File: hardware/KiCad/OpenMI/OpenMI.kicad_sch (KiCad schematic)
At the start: 0 parts

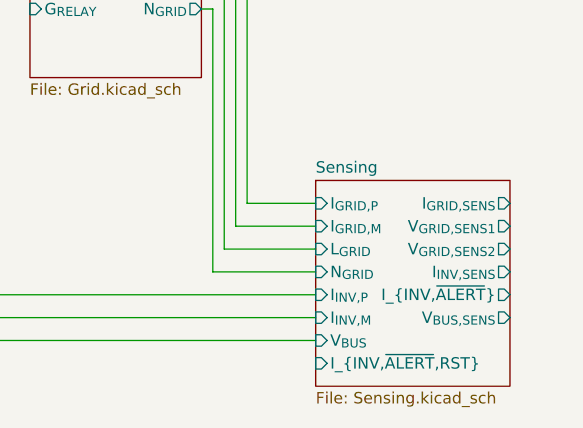
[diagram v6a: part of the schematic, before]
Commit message: feat(hw): Adds grid current alert output to `Sensing`.
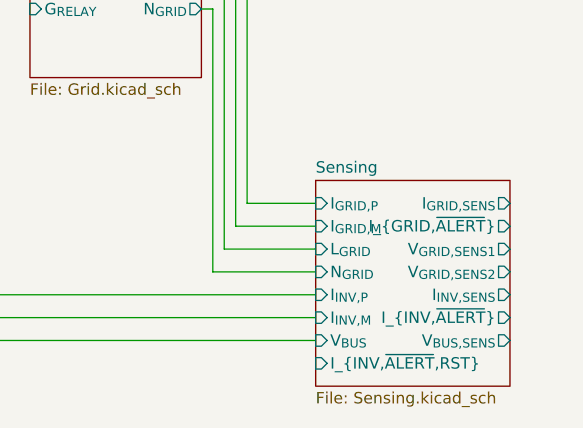
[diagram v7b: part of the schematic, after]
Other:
- sheet Sensing ports: added I_{GRID,~{ALERT}}; removed none
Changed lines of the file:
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@@
       (effects (font (size 1.27 1.27)) (justify left))
     )
-    (pin "I_{INV,~{ALERT}}" output (at 200.66 120.65 0)
+    (pin "I_{INV,~{ALERT}}" output (at 200.66 123.19 0)
       (effects (font (size 1.27 1.27)) (justify right))
     )
@@
       (effects (font (size 1.27 1.27)) (justify left))
     )
-    (pin "I_{INV,SENS}" output (at 200.66 118.11 0)
+    (pin "I_{INV,SENS}" output (at 200.66 120.65 0)
       (effects (font (size 1.27 1.27)) (justify right))
     )
@@
       (effects (font (size 1.27 1.27)) (justify left))
     )
-    (pin "V_{BUS,SENS}" output (at 200.66 123.19 0)
+    (pin "V_{BUS,SENS}" output (at 200.66 125.73 0)
       (effects (font (size 1.27 1.27)) (justify right))
     )
@@
       (effects (font (size 1.27 1.27)) (justify left))
     )
-    (pin "V_{GRID,SENS1}" output (at 200.66 113.03 0)
+    (pin "V_{GRID,SENS1}" output (at 200.66 115.57 0)
       (effects (font (size 1.27 1.27)) (justify right))
     )
-    (pin "V_{GRID,SENS2}" output (at 200.66 115.57 0)
+    (pin "V_{GRID,SENS2}" output (at 200.66 118.11 0)
       (effects (font (size 1.27 1.27)) (justify right))
     )
@@
       (effects (font (size 1.27 1.27)) (justify left))
     )
+    (pin "I_{GRID,~{ALERT}}" output (at 200.66 113.03 0)
+      (effects (font (size 1.27 1.27)) (justify right))
+    )
     (instances

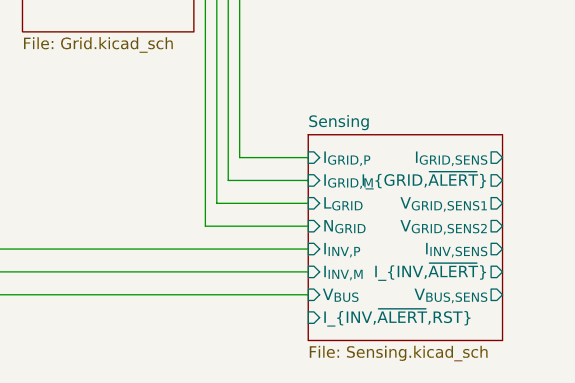
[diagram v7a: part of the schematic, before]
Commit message: feat(hw): Adds zero-crossing-detection (ZCD) to `Sensing`.
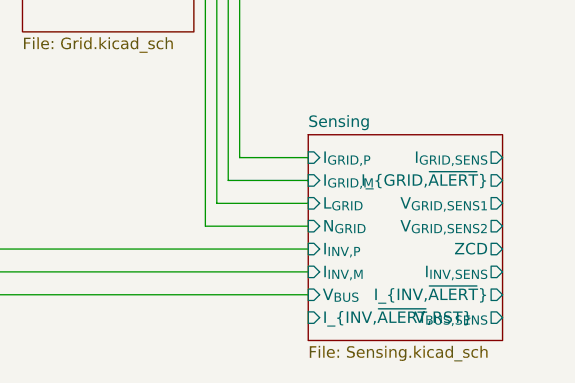
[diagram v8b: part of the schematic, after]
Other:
- sheet Sensing ports: added ZCD; removed none
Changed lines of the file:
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@@
       (effects (font (size 1.27 1.27)) (justify left))
     )
-    (pin "I_{INV,~{ALERT}}" output (at 200.66 123.19 0)
+    (pin "I_{INV,~{ALERT}}" output (at 200.66 125.73 0)
       (effects (font (size 1.27 1.27)) (justify right))
     )
@@
       (effects (font (size 1.27 1.27)) (justify left))
     )
-    (pin "I_{INV,SENS}" output (at 200.66 120.65 0)
+    (pin "I_{INV,SENS}" output (at 200.66 123.19 0)
       (effects (font (size 1.27 1.27)) (justify right))
     )
@@
       (effects (font (size 1.27 1.27)) (justify left))
     )
-    (pin "V_{BUS,SENS}" output (at 200.66 125.73 0)
+    (pin "V_{BUS,SENS}" output (at 200.66 128.27 0)
       (effects (font (size 1.27 1.27)) (justify right))
     )
@@
       (effects (font (size 1.27 1.27)) (justify right))
     )
+    (pin "ZCD" output (at 200.66 120.65 0)
+      (effects (font (size 1.27 1.27)) (justify right))
+    )
